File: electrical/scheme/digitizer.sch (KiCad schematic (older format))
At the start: 175 parts, among them P1 mode, P10 in-2, P11 in-3, P12 in-1, P13 USB_B, P14 screw, P15 screw, P16 screw, P17 screw, P2 ~rst~, P3 ext, P4 trig, P5 trig-mode, P6 swd, P7 out-0, P8 out-1, P9 in-0, U1 AD8672, U10 crystal-4pin, U100 AD8672, U101 AD8672, U11 CP2102, U12 adr4533, U13 BAT54S, U14 adr4533, U15 ADT7410, U16 MCP1703T-3302E/CB, U17 AD7683, U18 NCP3063, U19 ADG5204, U2 AD8672, U20 NCP3063, U3 AD8672

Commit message: a
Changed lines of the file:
@@
 Text Label 4150 5900 0    60   ~ 0
 led-0
-Text Label 9800 2300 0    60   ~ 0
+Text Label 9700 2300 0    60   ~ 0
 led-1
 $Comp

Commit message: Generated gerbers.
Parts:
- C101: value 220p -> 100p
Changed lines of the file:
@@
 P 22850 7000
 F 0 "C101" H 22875 7100 50  0000 L CNN
-F 1 "220p" H 22875 6900 50  0000 L CNN
+F 1 "100p" H 22875 6900 50  0000 L CNN
 F 2 "Capacitors_SMD:C_0805_HandSoldering" H 22888 6850 30  0001 C CNN
 F 3 "" H 22850 7000 60  0000 C CNN

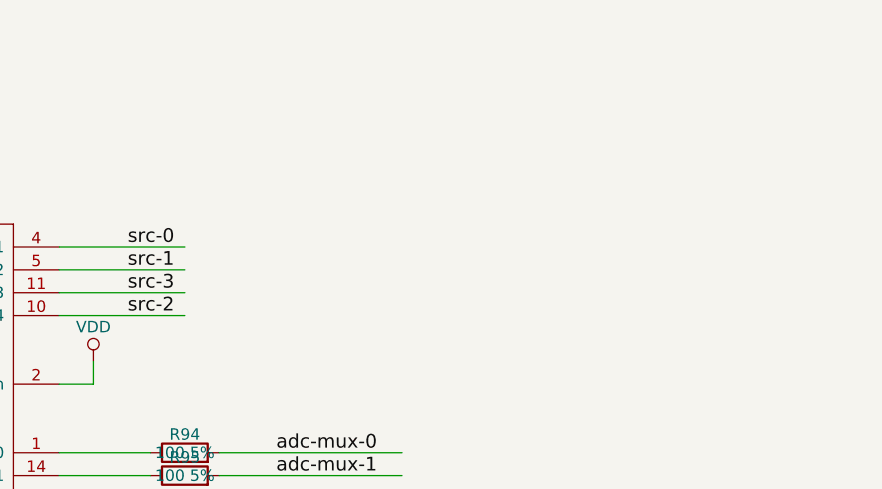
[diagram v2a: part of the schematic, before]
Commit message: Added some improvements. But if just 1kOhm resistor added in between filter and multiplexer it solves switch spike back propagation into filter. And it eliminates mutual signal interference.
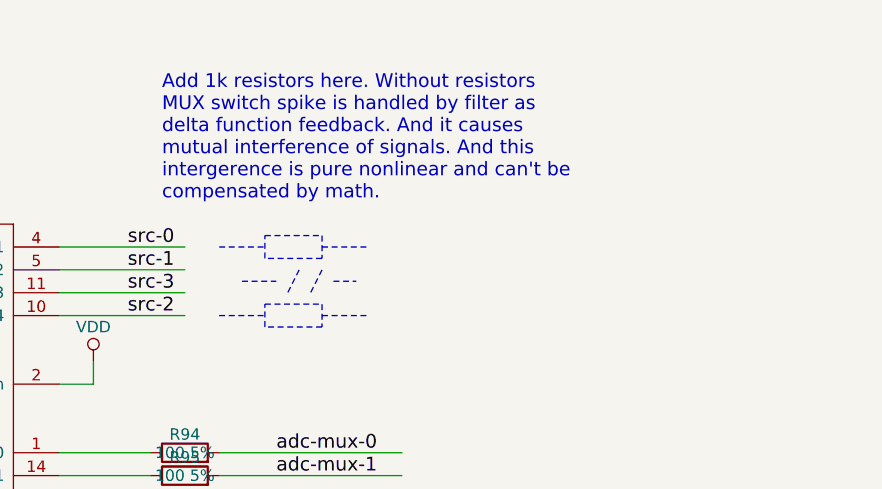
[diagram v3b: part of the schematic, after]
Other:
- note added: "Add 1k resistors here. Without resistors \nMUX switch spike is handled by filter as \ndelta function feedback. And it causes \nmutual interference of signals. And this \nintergerence is pure nonlinear and can't be \ncompensated by math."
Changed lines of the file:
@@
 NoConn ~ 7850 16700
 NoConn ~ 7850 15150
+Wire Notes Line
+	23600 1650 23800 1650
+Wire Notes Line
+	23800 1700 23800 1600
+Wire Notes Line
+	23800 1600 24050 1600
+Wire Notes Line
+	24050 1600 24050 1700
+Wire Notes Line
+	24050 1700 23800 1700
+Wire Notes Line
+	24050 1650 24250 1650
+Wire Notes Line
+	23700 1800 23850 1800
+Wire Notes Line
+	23950 1750 23900 1850
+Wire Notes Line
+	24050 1750 24000 1850
+Wire Notes Line
+	24100 1800 24200 1800
+Wire Notes Line
+	23600 1950 23800 1950
+Wire Notes Line
+	23800 2000 23800 1900
+Wire Notes Line
+	23800 1900 24050 1900
+Wire Notes Line
+	24050 1900 24050 2000
+Wire Notes Line
+	24050 2000 23800 2000
+Wire Notes Line
+	24050 1950 24250 1950
+Text Notes 23350 1450 0    60   ~ 0
+Add 1k resistors here. Without resistors \nMUX switch spike is handled by filter as \ndelta function feedback. And it causes \nmutual interference of signals. And this \nintergerence is pure nonlinear and can't be \ncompensated by math.
 $EndSCHEMATC

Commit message: a
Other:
- note added: "It's most probably that feedback \nshould be read directly after the \nSchottky but not after filter."
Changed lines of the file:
@@
 Text Notes 23350 1450 0    60   ~ 0
 Add 1k resistors here. Without resistors \nMUX switch spike is handled by filter as \ndelta function feedback. And it causes \nmutual interference of signals. And this \nintergerence is pure nonlinear and can't be \ncompensated by math.
+Text Notes 14400 21400 0    60   ~ 0
+It's most probably that feedback \nshould be read directly after the \nSchottky but not after filter.
+Wire Notes Line
+	13700 21000 14750 20850
+Wire Notes Line
+	14750 20850 14800 19100
+Wire Notes Line
+	14750 20850 19150 20400
+Wire Notes Line
+	19150 20400 19050 19100
 $EndSCHEMATC
